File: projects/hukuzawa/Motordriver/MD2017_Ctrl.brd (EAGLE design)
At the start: 70 x 70 mm, 18 parts, among them IC1 PIC16F648, J1 3X2A, Q1 CERALOCK

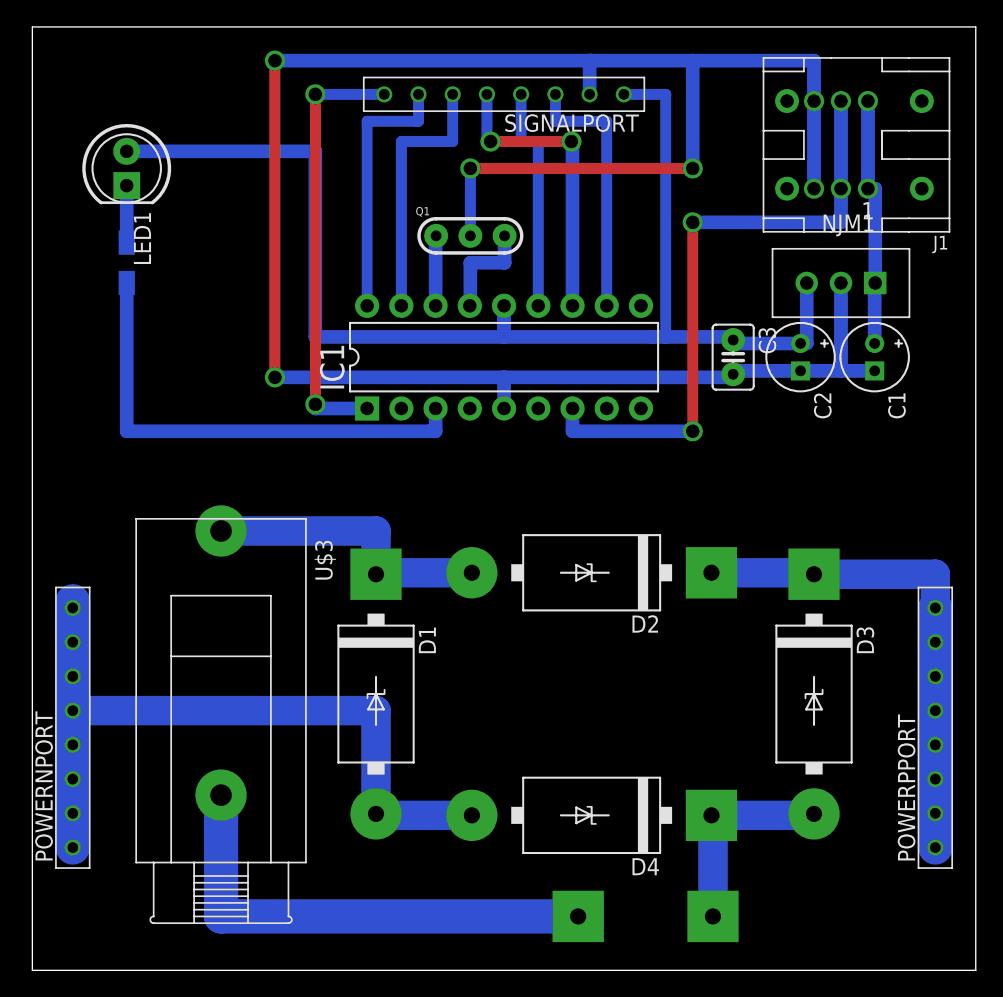
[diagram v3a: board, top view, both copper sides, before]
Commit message: モータードライバ全ボード図修正
配置の基準単位をmilに変更して再配置・再配線
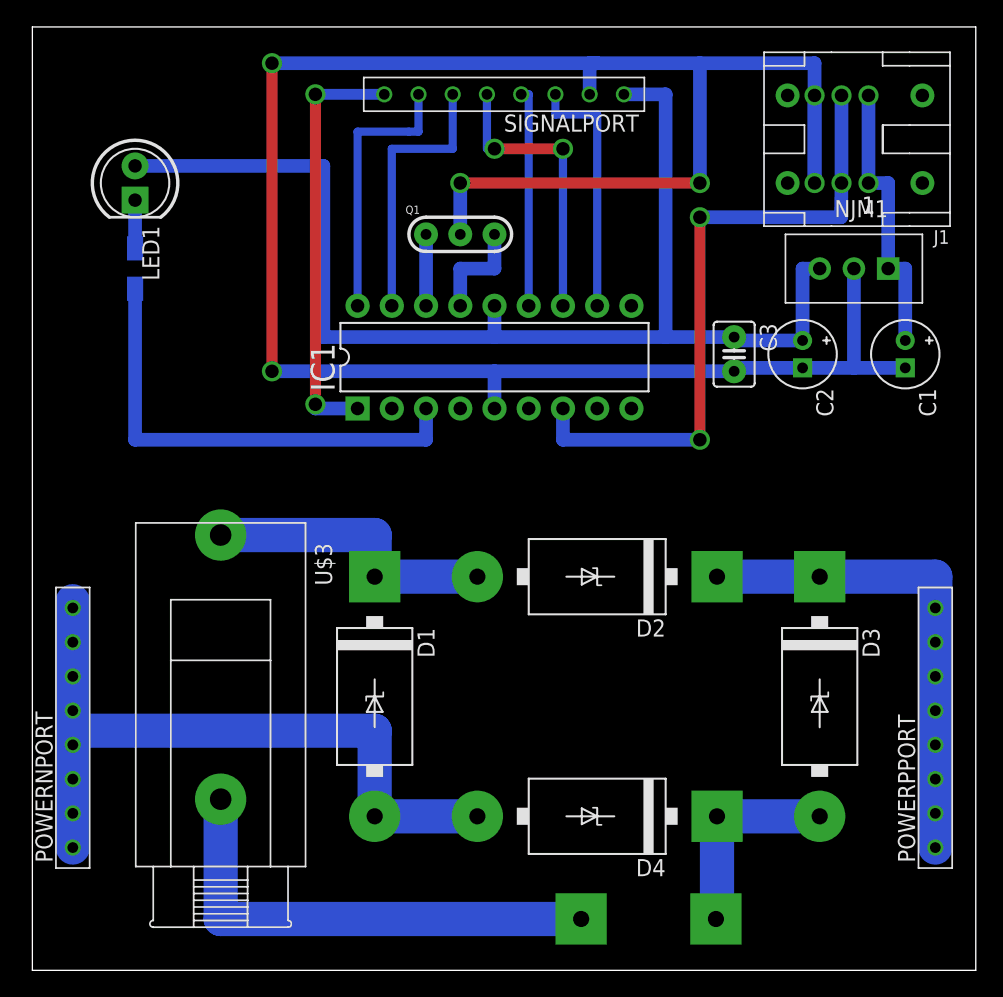
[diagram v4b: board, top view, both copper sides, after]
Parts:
- C1, C2: value (none) -> 47uF
- R1: value (none) -> 1k
- moved C1 2.28 mm to (64.8, 45.7)
- moved NJM1 1.44 mm to (61.0, 52.1)
- moved LED1 1.25 mm to (7.62, 58.4)
- moved Q1 0.76 mm to (31.8, 54.6)
- moved R1 0.75 mm to (7.62, 52.1)
- moved IC1 0.71 mm to (34.3, 45.5)
- moved D2 0.50 mm to (41.9, 29.2)
- moved D3 0.46 mm to (58.4, 20.3)
- moved J1 0.42 mm to (66.0, 58.4)
- moved D4 0.42 mm to (41.9, 11.4)
- moved U$3 0.30 mm to (14.0, 12.7)
- moved U$2 0.29 mm to (45.7, 3.81)
- moved C2 0.27 mm to (57.1, 45.7)
- moved C3 0.23 mm to (52.1, 45.7)
- moved D1 0.21 mm to (25.4, 20.3)
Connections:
- net 5V renamed VDD5V
- net N$3 renamed GND2
- net N$4 renamed BATTA
- net N$6 renamed BATTB
- net N$7 renamed VCC12V
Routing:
- net GND: track 159.0 -> 169.2 mm
- net VDD5V: track 94.9 -> 92.5 mm
- net SIGNAL: track 46.1 -> 48.5 mm
- net 9VIN: track 18.6 -> 20.9 mm
- net GND2: track 55.7 -> 54.7 mm
- net BDIR: track 32.3 -> 31.6 mm
- net BD/B: track 19.5 -> 20.2 mm
- net APWM: track 19.5 -> 18.8 mm
- net ADIR: track 22.0 -> 21.3 mm
- net AD/B: track 17.0 -> 16.2 mm
- net BPWM: track 19.5 -> 20.2 mm
- net VCC12V: track 37.0 -> 36.3 mm
- net N$1: track 4.23 -> 3.58 mm

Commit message: モータードライバ修正
すべての配線の名前を変更
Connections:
- net N$1 renamed NLED1
- net N$5 renamed NBATT1
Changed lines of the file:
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@@
 <wire x1="49.53" y1="58.42" x2="49.53" y2="67.31" width="1.016" layer="16"/>
 </signal>
-<signal name="N$1">
+<signal name="NLED1">
 <contactref element="R1" pad="2"/>
 <contactref element="LED1" pad="K"/>
@@
 <wire x1="25.4" y1="17.78" x2="3" y2="17.78" width="2.54" layer="16"/>
 </signal>
-<signal name="N$5">
+<signal name="NBATT1">
 <contactref element="U$3" pad="1"/>
 <contactref element="D1" pad="C"/>

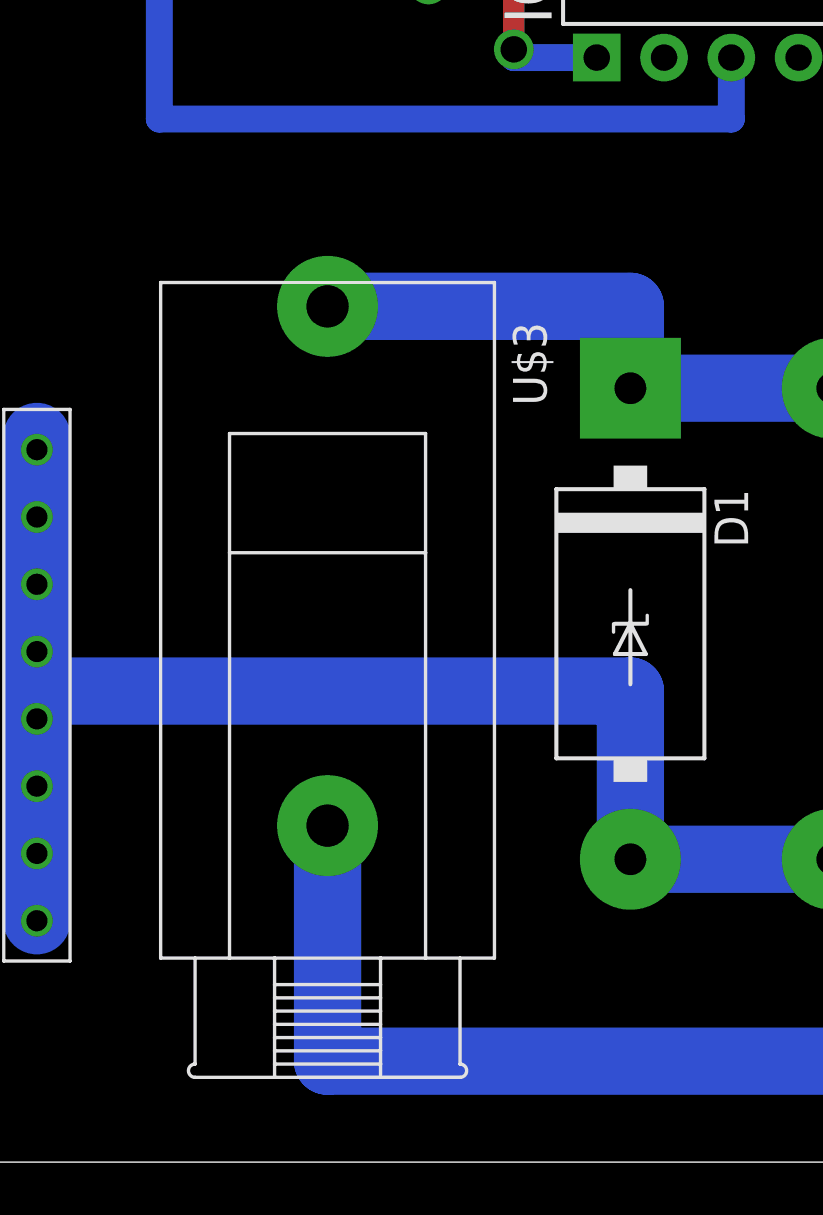
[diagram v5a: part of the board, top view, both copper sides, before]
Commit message: モータードライバ修正
使用ヒューズホルダー変更
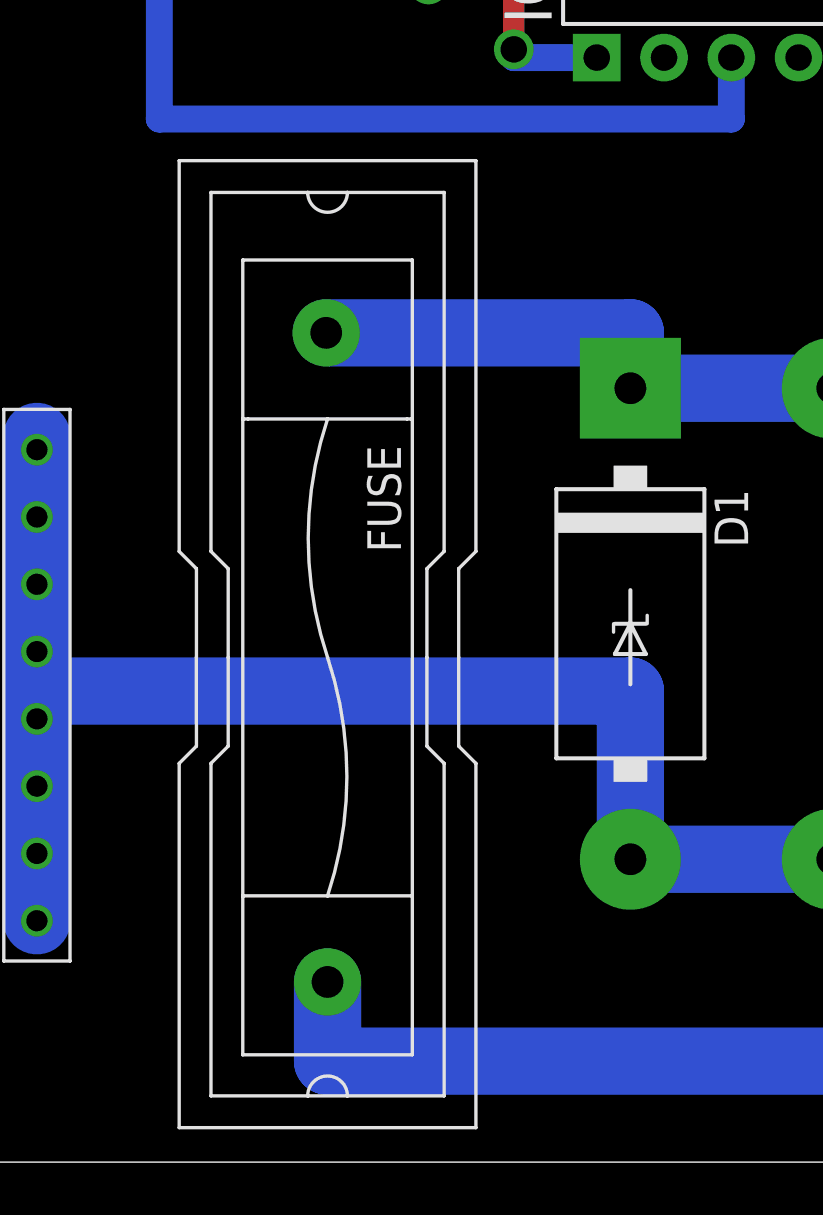
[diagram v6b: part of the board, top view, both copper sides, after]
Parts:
- removed U$3: F-115, testLib:F-115
- added FUSE: MF-550C, MF5xx:MF550C
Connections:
- removed net NBATT1: D1.C, D2.A, U$3.1
- new net N$1: D1.C, D2.A, FUSE.PA
- net BATTA: now also FUSE.PB; no longer U$3.2
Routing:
- net NBATT1: track 22.1 -> 0.00 mm
- net N$1: track 0.00 -> 21.2 mm
- net BATTA: track 35.6 -> 29.7 mm
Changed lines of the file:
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@@
 <element name="R1" library="rcl" package="R3216W" value="1k" x="7.62" y="52.07" rot="MR90"/>
 <element name="U$2" library="Powerio" package="2P" value="2P" x="45.72" y="3.81" rot="R180"/>
-<element name="U$3" library="testLib" package="F-115" value="F-115" x="13.97" y="12.7" rot="R270"/>
 <element name="C1" library="FP-21T for MITS" package="E2-5" value="47uF" x="64.77" y="45.72" rot="R270"/>
 <element name="C2" library="FP-21T for MITS" package="E2-5" value="47uF" x="57.15" y="45.72" rot="R270"/>
@@
 <element name="D3" library="diode" package="DO201-15" value="Z-DIODE" x="58.42" y="20.32" rot="R270"/>
 <element name="D4" library="diode" package="DO201-15" value="Z-DIODE" x="41.91" y="11.43" rot="R180"/>
+<element name="FUSE" library="MF5xx" package="MF550C" value="MF-550C" x="13.97" y="19.05" rot="R270"/>
 </elements>
 <signals>
@@
 <wire x1="25.4" y1="17.78" x2="3" y2="17.78" width="2.54" layer="16"/>
 </signal>
-<signal name="NBATT1">
-<contactref element="U$3" pad="1"/>
-<contactref element="D1" pad="C"/>
-<contactref element="D2" pad="A"/>
-<wire x1="33.02" y1="29.21" x2="25.4" y2="29.21" width="2.54" layer="16"/>
-<wire x1="25.4" y1="32.3" x2="25.4" y2="29.21" width="2.54" layer="16"/>
-<wire x1="25.4" y1="32.3" x2="13.97" y2="32.3" width="2.54" layer="16"/>
-</signal>
 <signal name="BATTB">
 <contactref element="U$2" pad="P1"/>
@@
 </signal>
 <signal name="BATTA">
-<contactref element="U$3" pad="2"/>
 <contactref element="U$2" pad="P2"/>
-<wire x1="13.97" y1="12.7" x2="13.97" y2="3.81" width="2.54" layer="16"/>
 <wire x1="13.97" y1="3.81" x2="40.72" y2="3.81" width="2.54" layer="16"/>
+<contactref element="FUSE" pad="PB"/>
+<wire x1="13.97" y1="6.8" x2="13.97" y2="3.81" width="2.54" layer="16"/>
+</signal>
+<signal name="N$1">
+<contactref element="D1" pad="C"/>
+<contactref element="D2" pad="A"/>
+<wire x1="33.02" y1="29.21" x2="25.4" y2="29.21" width="2.54" layer="16"/>
+<contactref element="FUSE" pad="PA"/>
+<wire x1="25.4" y1="29.21" x2="25.4" y2="31.3" width="2.54" layer="16"/>
+<wire x1="25.4" y1="31.3" x2="13.92" y2="31.3" width="2.54" layer="16"/>
 </signal>
 </signals>
